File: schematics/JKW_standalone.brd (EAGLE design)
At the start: 159.4 x 80.7 mm, 229 parts, among them IC1 4093D, IC4 ATMEGA2560-16AU, Q1 BSS84, Q10 BSS84, Q11 BSS84, Q2 BSS84, Q3 BSS84, Q4 BSS84, Q5 BSS84, Q6 BSS84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

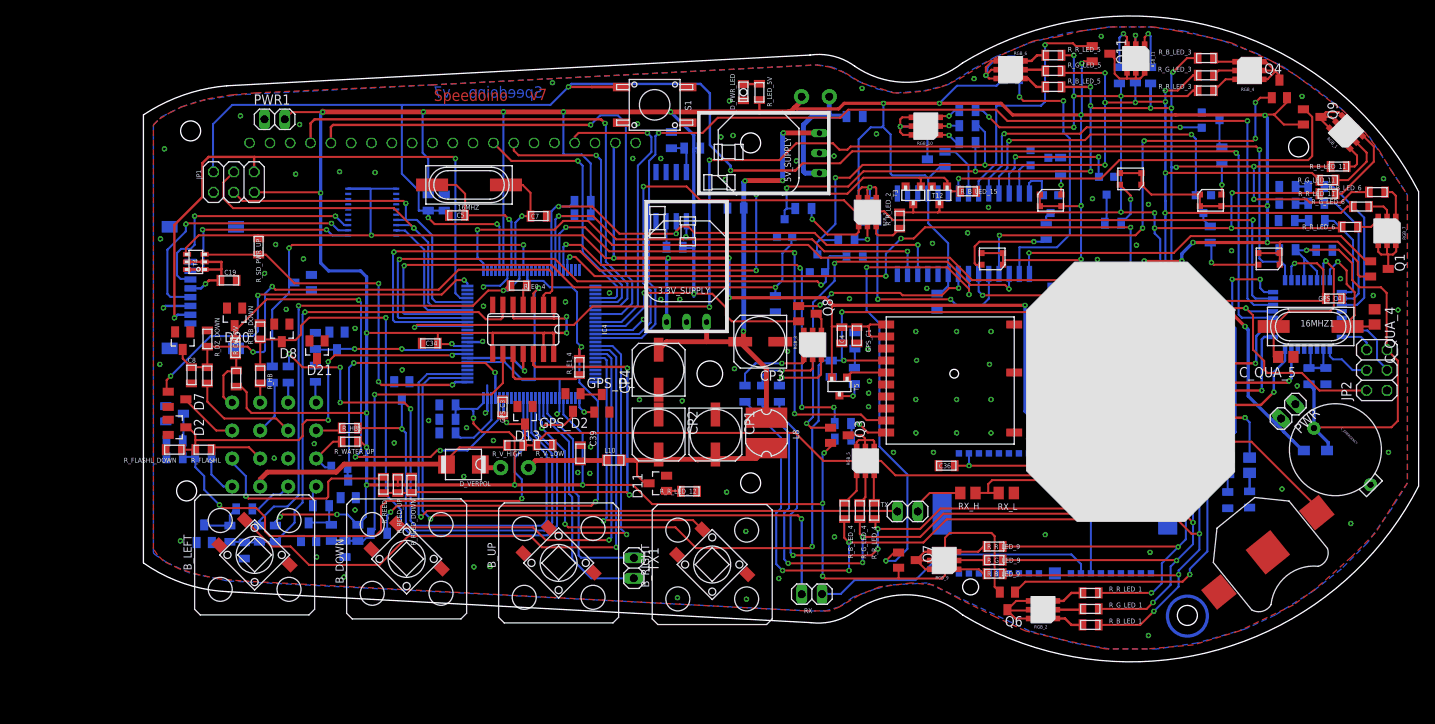
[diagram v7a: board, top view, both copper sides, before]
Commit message: added pads for light sensor
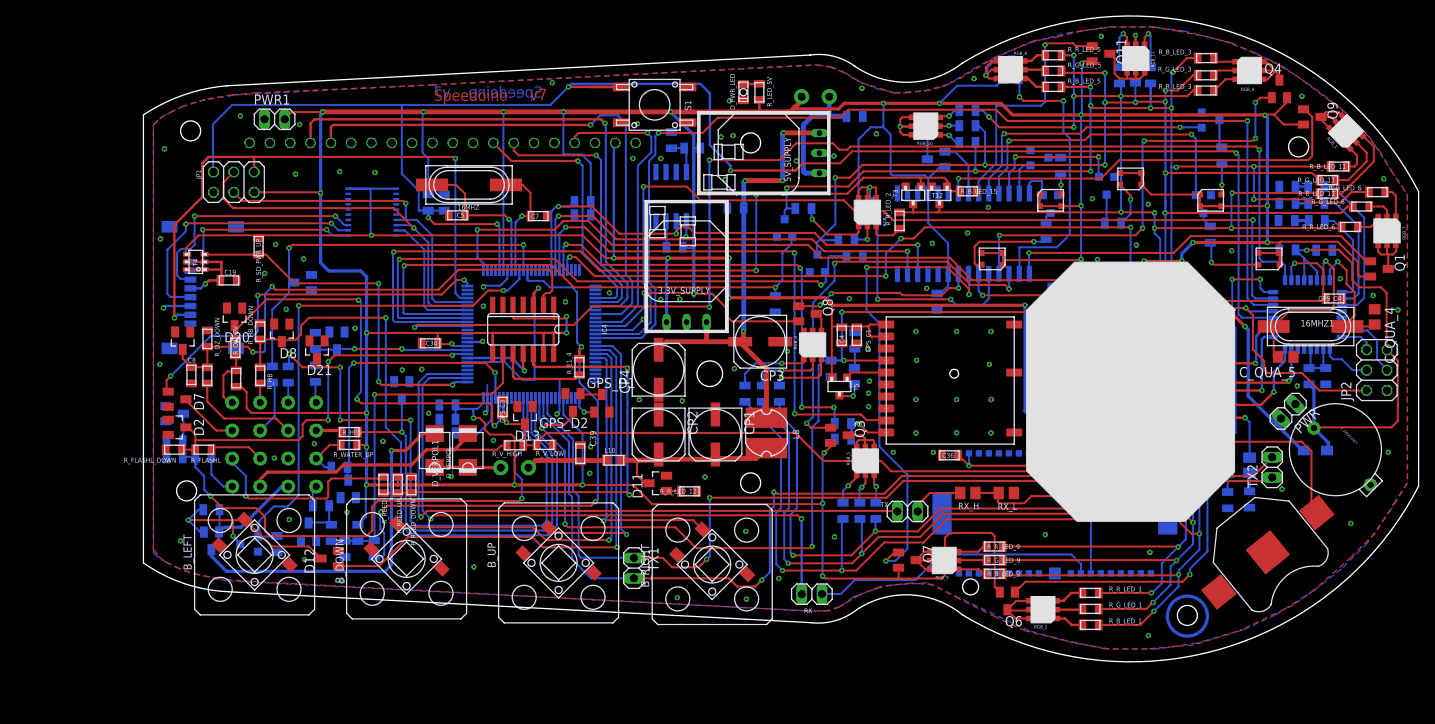
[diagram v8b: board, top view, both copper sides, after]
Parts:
- removed D_P_EX_D2: 78-MMBZ5232B-V, diode:SOT23
- removed R_E0_0, R_E0_2, R_E0_4: n.b., RCLDT:0805
- removed R_E0_1, R_E0_3: n.b. / 0R, RCLDT:0805
- removed R_HB2: 600R, RCLDT:0805
- added D12: 771-PMBD7000235, semicon-smd-ipc:SOT23
- added D_VERPOL1: SS24T3G, RCLDT:SMB
- added R_DEAKT_DAUER_P, R_DEAKT_DAUER_P1: 10k, RCLDT:0805
- added T13: Mouser: 771-2N7002BK215 , N-Channel, 60V 350mA, SOT-23, 0,0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, RCLDT:SOT-23
- added TX2: (no value), pinhead:1X02
- added T_P_BRIDGE: PMV160UP215, Kolja:SOT23
- moved R_E1_2 2.00 mm to (28.9, 9.55), turned to 270 degrees
- moved D_VERPOL 1.83 mm to (40.5, 21.8), turned to 270 degrees
- moved C36 1.36 mm to (100.8, 21.2)
- moved R_HB5 0.50 mm to (25.8, 24.1)
- moved R_WATER_UP 0.41 mm to (25.7, 22.5)
- moved R_B_LED_4 0.20 mm to (87.5, 14.2), flipped to the bottom
- moved R_R_LED_4 0.20 mm to (91.5, 14.2), flipped to the bottom
- flipped R_G_LED_4 to the bottom
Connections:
- removed net D49: IC4.35, R_E0_2.2, R_E0_4.2
- removed net N$24: 12V_F1.P$1, D_VERPOL.K
- removed net N$46: IC1.4, R_E0_4.1
- removed net N$89: R_HB2.1, SPEEDOSTECKER.P$14
- new net 12V_D_SAFE: 12V_F1.P$1, D_VERPOL.K, D_VERPOL1.K
- new net 12V_PERMANENT: R_DEAKT_DAUER_P.1, SPEEDOSTECKER.P$14, T_P_BRIDGE.2
- new net SELF_PWR_UP: IC4.35, R_DEAKT_DAUER_P1.1, T13.1
- net A12: now also TX2.2
- net A13: now also TX2.1
- net B_LEFT: now also D12.3, R_DEAKT_DAUER_P.2, T13.3, T_P_BRIDGE.1; no longer IC4.67
- net GND: now also R_DEAKT_DAUER_P1.2, T13.2; no longer D_P_EX_D2.1, R_E0_3.1
- net N$41: now also D12.1, IC4.67; no longer D_P_EX_D2.3, R_E0_1.1, R_HB2.2
- net N$45: now also D_VERPOL1.A, T_P_BRIDGE.3; no longer IC1.6, R_E0_0.1, R_E0_1.2, R_E0_2.1, R_E0_3.2
- net VDD: no longer IC1.5, R_E0_0.2
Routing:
- net A12: track 30.3 -> 123.0 mm, vias 0 -> 2
- net A13: track 28.3 -> 117.5 mm, vias 0 -> 2
- net SELF_PWR_UP: track 0.00 -> 64.5 mm, vias 0 -> 2
- net D49: track 61.7 -> 0.00 mm, vias 2 -> 0
- net N$41: track 5.64 -> 63.6 mm, vias 0 -> 1
- net B_LEFT: track 77.6 -> 27.1 mm, vias 1 -> 2
- net N$45: track 62.9 -> 45.0 mm
- net 12V_PERMANENT: track 0.00 -> 13.9 mm
- net VDD: track 765.4 -> 751.9 mm, vias 38 -> 36
- net 12V_D_SAFE: track 0.00 -> 8.30 mm
- net A1: track 62.4 -> 56.3 mm
- net N$89: track 5.64 -> 0.00 mm
- net D47: track 66.3 -> 71.5 mm
- net N$11: track 31.5 -> 35.3 mm
- net A2: track 149.2 -> 146.4 mm
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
